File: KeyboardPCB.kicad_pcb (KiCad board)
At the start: 2 copper layers, 304.8 x 100 mm, 155 parts, among them J1 AVR-ISP-6, SW1 GRV, SW10 #9, SW11 #0, SW12 -_, SW13 =+, SW14 BSPC, SW15 PGUP, SW16 TAB, SW17 Q, SW18 W, SW19 E, SW2 #1, SW20 R, SW21 T, SW22 Y, SW23 U, SW24 I, SW25 O, SW26 P, SW27 [{, SW28 ]}, SW29 \|, SW3 #2, SW30 PGDN, SW31 CAPSLOCK, SW32 A, SW33 S, SW34 D, SW35 F, SW36 G, SW37 H, SW38 J, SW39 K, SW4 #3, SW40 L, SW41 ;:, SW42 '", SW43 ENTER, SW44 INS, SW45 LSHIFT, SW46 Z, SW47 X, SW48 C, SW49 V, SW5 #4, SW50 B, SW51 N, SW52 M, SW53 ,<, SW54 .>, SW55 /?, SW56 RSHIFT, SW57 UP, SW58 DEL, SW59 LCTRL, SW6 #5, SW60 LALT, SW61 LCOMMAND, SW62 SPACE, SW63 RCOMMAND, SW64 RALT, SW65 LEFT, SW66 DOWN, SW67 RIGHT, SW68 SW_SKQG, SW7 #6, SW8 #7, SW9 #8, U1 ATmega32U4-A, Y1 Crystal_GND24_Small

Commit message: Routed about half of the PCB
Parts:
- moved D27 11.0 mm to (287.3, 102.1)
- moved D30 11.0 mm to (353.2, 102.1)
- moved D20 11.0 mm to (153.2, 102.1)
- moved D21 11.0 mm to (172.2, 102.1)
- moved D22 11.0 mm to (191.3, 102.1)
- moved D23 11.0 mm to (210.3, 102.1)
- moved D24 11.0 mm to (229.4, 102.1)
- moved D25 11.0 mm to (248.4, 102.1)
- moved D16 11.0 mm to (72.2, 102.1)
- moved D17 11.0 mm to (96.0, 102.2)
- moved D18 11.0 mm to (115.1, 102.1)
- moved D19 11.0 mm to (134.1, 102.1)
- moved D26 11.0 mm to (268.3, 102.1)
- moved D28 11.0 mm to (305.6, 102.1)
- moved D29 11.0 mm to (329.4, 102.1)
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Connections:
- net Net-(D0-I/O1) renamed DP
- net Net-(D0-I/O2) renamed DN
- SW1 pad 1: Net-(D1-A) -> col0
- SW1 pad 2: col0 -> Net-(D1-A)
- SW10 pad 1: Net-(D10-A) -> col9
- SW10 pad 2: col9 -> Net-(D10-A)
- SW11 pad 1: Net-(D11-A) -> col10
- SW11 pad 2: col10 -> Net-(D11-A)
- SW12 pad 1: Net-(D12-A) -> col11
- SW12 pad 2: col11 -> Net-(D12-A)
- SW13 pad 1: Net-(D13-A) -> col12
- SW13 pad 2: col12 -> Net-(D13-A)
- SW14 pad 1: Net-(D14-A) -> col13
- SW14 pad 2: col13 -> Net-(D14-A)
- SW15 pad 1: Net-(D15-A) -> col14
- SW15 pad 2: col14 -> Net-(D15-A)
- SW16 pad 1: Net-(D16-A) -> col0
- SW16 pad 2: col0 -> Net-(D16-A)
- SW17 pad 1: Net-(D17-A) -> col1
- SW17 pad 2: col1 -> Net-(D17-A)
- SW18 pad 1: Net-(D18-A) -> col2
- SW18 pad 2: col2 -> Net-(D18-A)
- SW19 pad 1: Net-(D19-A) -> col3
- SW19 pad 2: col3 -> Net-(D19-A)
- SW2 pad 1: Net-(D2-A) -> col1
- SW2 pad 2: col1 -> Net-(D2-A)
- SW20 pad 1: Net-(D20-A) -> col4
- SW20 pad 2: col4 -> Net-(D20-A)
- SW21 pad 1: Net-(D21-A) -> col5
- SW21 pad 2: col5 -> Net-(D21-A)
- SW22 pad 1: Net-(D22-A) -> col6
- SW22 pad 2: col6 -> Net-(D22-A)
- SW23 pad 1: Net-(D23-A) -> col7
- SW23 pad 2: col7 -> Net-(D23-A)
- SW24 pad 1: Net-(D24-A) -> col8
- SW24 pad 2: col8 -> Net-(D24-A)
- SW25 pad 1: Net-(D25-A) -> col9
- SW25 pad 2: col9 -> Net-(D25-A)
- SW26 pad 1: Net-(D26-A) -> col10
- SW26 pad 2: col10 -> Net-(D26-A)
- SW27 pad 1: Net-(D27-A) -> col11
- SW27 pad 2: col11 -> Net-(D27-A)
- SW28 pad 1: Net-(D28-A) -> col12
- SW28 pad 2: col12 -> Net-(D28-A)
- SW29 pad 1: Net-(D29-A) -> col13
- SW29 pad 2: col13 -> Net-(D29-A)
- SW3 pad 1: Net-(D3-A) -> col2
- SW3 pad 2: col2 -> Net-(D3-A)
- SW30 pad 1: Net-(D30-A) -> col14
- SW30 pad 2: col14 -> Net-(D30-A)
- SW31 pad 1: Net-(D31-A) -> col0
- SW31 pad 2: col0 -> Net-(D31-A)
- SW32 pad 1: Net-(D32-A) -> col1
- SW32 pad 2: col1 -> Net-(D32-A)
- SW33 pad 1: Net-(D33-A) -> col2
- SW33 pad 2: col2 -> Net-(D33-A)
- SW34 pad 1: Net-(D34-A) -> col3
- SW34 pad 2: col3 -> Net-(D34-A)
- SW35 pad 1: Net-(D35-A) -> col4
- SW35 pad 2: col4 -> Net-(D35-A)
- SW36 pad 1: Net-(D36-A) -> col5
- SW36 pad 2: col5 -> Net-(D36-A)
- SW37 pad 1: Net-(D37-A) -> col6
- SW37 pad 2: col6 -> Net-(D37-A)
- SW38 pad 1: Net-(D38-A) -> col7
- SW38 pad 2: col7 -> Net-(D38-A)
- SW39 pad 1: Net-(D39-A) -> col8
- SW39 pad 2: col8 -> Net-(D39-A)
- SW4 pad 1: Net-(D4-A) -> col3
- SW4 pad 2: col3 -> Net-(D4-A)
- SW40 pad 1: Net-(D40-A) -> col9
- SW40 pad 2: col9 -> Net-(D40-A)
- SW41 pad 1: Net-(D41-A) -> col10
- SW41 pad 2: col10 -> Net-(D41-A)
- SW42 pad 1: Net-(D42-A) -> col11
- SW42 pad 2: col11 -> Net-(D42-A)
- SW43 pad 1: Net-(D43-A) -> col13
- SW43 pad 2: col13 -> Net-(D43-A)
- SW44 pad 1: Net-(D44-A) -> col14
- SW44 pad 2: col14 -> Net-(D44-A)
- SW45 pad 1: Net-(D45-A) -> col0
- SW45 pad 2: col0 -> Net-(D45-A)
- SW46 pad 1: Net-(D46-A) -> col1
- SW46 pad 2: col1 -> Net-(D46-A)
- SW47 pad 1: Net-(D47-A) -> col2
- SW47 pad 2: col2 -> Net-(D47-A)
- SW48 pad 1: Net-(D48-A) -> col3
- SW48 pad 2: col3 -> Net-(D48-A)
- SW49 pad 1: Net-(D49-A) -> col4
- SW49 pad 2: col4 -> Net-(D49-A)
- SW5 pad 1: Net-(D5-A) -> col4
- SW5 pad 2: col4 -> Net-(D5-A)
- SW50 pad 1: Net-(D50-A) -> col5
- SW50 pad 2: col5 -> Net-(D50-A)
- SW51 pad 1: Net-(D51-A) -> col6
- SW51 pad 2: col6 -> Net-(D51-A)
- SW52 pad 1: Net-(D52-A) -> col7
- SW52 pad 2: col7 -> Net-(D52-A)
- SW53 pad 1: Net-(D53-A) -> col8
- SW53 pad 2: col8 -> Net-(D53-A)
- SW54 pad 1: Net-(D54-A) -> col9
- SW54 pad 2: col9 -> Net-(D54-A)
- SW55 pad 1: Net-(D55-A) -> col10
- SW55 pad 2: col10 -> Net-(D55-A)
- SW56 pad 1: Net-(D56-A) -> col12
- SW56 pad 2: col12 -> Net-(D56-A)
- SW57 pad 1: Net-(D57-A) -> col13
- SW57 pad 2: col13 -> Net-(D57-A)
- SW58 pad 1: Net-(D58-A) -> col14
- SW58 pad 2: col14 -> Net-(D58-A)
- SW59 pad 1: Net-(D59-A) -> col0
- SW59 pad 2: col0 -> Net-(D59-A)
- SW6 pad 1: Net-(D6-A) -> col5
- SW6 pad 2: col5 -> Net-(D6-A)
- SW60 pad 1: Net-(D60-A) -> col1
- SW60 pad 2: col1 -> Net-(D60-A)
- SW61 pad 1: Net-(D61-A) -> col2
- SW61 pad 2: col2 -> Net-(D61-A)
- SW62 pad 1: Net-(D62-A) -> col6
- SW62 pad 2: col6 -> Net-(D62-A)
- SW63 pad 1: Net-(D63-A) -> col10
- SW63 pad 2: col10 -> Net-(D63-A)
- SW64 pad 1: Net-(D64-A) -> col11
- SW64 pad 2: col11 -> Net-(D64-A)
- SW65 pad 1: Net-(D65-A) -> col12
- SW65 pad 2: col12 -> Net-(D65-A)
- SW66 pad 1: Net-(D66-A) -> col13
- SW66 pad 2: col13 -> Net-(D66-A)
- SW67 pad 1: Net-(D67-A) -> col14
- SW67 pad 2: col14 -> Net-(D67-A)
- SW7 pad 1: Net-(D7-A) -> col6
- SW7 pad 2: col6 -> Net-(D7-A)
- SW8 pad 1: Net-(D8-A) -> col7
- SW8 pad 2: col7 -> Net-(D8-A)
- SW9 pad 1: Net-(D9-A) -> col8
- SW9 pad 2: col8 -> Net-(D9-A)
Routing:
- net row0: track 0.00 -> 268.9 mm
- net row1: track 0.00 -> 261.9 mm
- net row2: track 0.00 -> 259.6 mm
- net row3: track 0.00 -> 254.9 mm
- net row4: track 0.00 -> 209.7 mm
- net col1: track 0.00 -> 90.9 mm
- net col10: track 0.00 -> 89.9 mm
- net col2: track 0.00 -> 88.0 mm
- net col6: track 0.00 -> 87.9 mm
- net col13: track 0.00 -> 86.1 mm
- net col11: track 0.00 -> 84.4 mm
- net col0: track 0.00 -> 84.1 mm
- net col12: track 0.00 -> 84.0 mm
- net col14: track 0.00 -> 76.2 mm
- net DP: track 0.00 -> 73.9 mm
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- added copper zone on B.Cu, net GND
- added copper zone on F.Cu, net GND

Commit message: Routed around MCU
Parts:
- removed C6: 0.1u, Capacitor_SMD:C_0805_2012Metric
- moved D9 11.5 mm to (219.6, 83.6)
- moved R1 3.25 mm to (210.6, 162.8)
- moved C2 2.27 mm to (231.3, 156.5)
- moved Y1 2.27 mm to (227.8, 155.4)
- moved C3 2.27 mm to (231.3, 154.3)
- moved C7 1.75 mm to (227.8, 151.0), turned to 0 degrees
- moved C8 1.02 mm to (208.3, 145.8)
- moved C5 0.56 mm to (206.6, 158.2), turned to 90 degrees
- turned R5 to 0 degrees
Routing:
- net GND: track 23.5 -> 180.1 mm, vias 3 -> 8
- net +5V: track 5.85 -> 149.6 mm, vias 0 -> 6
- net VCC: track 0.00 -> 22.4 mm, vias 0 -> 2
- net row2: track 259.6 -> 278.6 mm, vias 0 -> 2
- net row0: track 268.9 -> 287.5 mm, vias 0 -> 2
- net Net-(USB1-CC1): track 0.00 -> 6.13 mm
- net Net-(USB1-CC2): track 0.00 -> 5.88 mm
- net Net-(D9-A): track 11.5 -> 6.52 mm
- net Net-(U1-UCAP): track 0.00 -> 4.38 mm
- net col8: track 66.9 -> 69.2 mm
- net XTAL1: track 12.4 -> 10.6 mm
- net XTAL2: track 11.0 -> 9.15 mm

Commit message: Continued routing
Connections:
- U1 pad 1: row0 -> row3
- U1 pad 36: col6 -> row4
- U1 pad 38: row1 -> col6
- U1 pad 39: row4 -> row0
- U1 pad 40: row3 -> row1
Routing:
- net col0: track 84.1 -> 247.0 mm, vias 0 -> 1
- net col14: track 76.2 -> 215.5 mm, vias 0 -> 1
- net col1: track 90.9 -> 225.6 mm, vias 0 -> 1
- net col13: track 86.1 -> 204.9 mm, vias 0 -> 1
- net col2: track 88.0 -> 194.7 mm, vias 0 -> 1
- net col12: track 84.0 -> 179.5 mm, vias 0 -> 1
- net col3: track 66.9 -> 156.7 mm, vias 0 -> 1
- net row4: track 209.7 -> 295.2 mm, vias 0 -> 2
- net col11: track 84.4 -> 161.8 mm, vias 0 -> 1
- net col4: track 66.9 -> 136.5 mm, vias 0 -> 1
- net col9: track 66.9 -> 115.4 mm, vias 0 -> 1
- net col10: track 89.9 -> 136.7 mm, vias 0 -> 1
- net col5: track 66.9 -> 113.4 mm, vias 0 -> 1
- net col8: track 69.2 -> 108.4 mm, vias 0 -> 1
- net row3: track 254.9 -> 289.8 mm, vias 0 -> 4
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
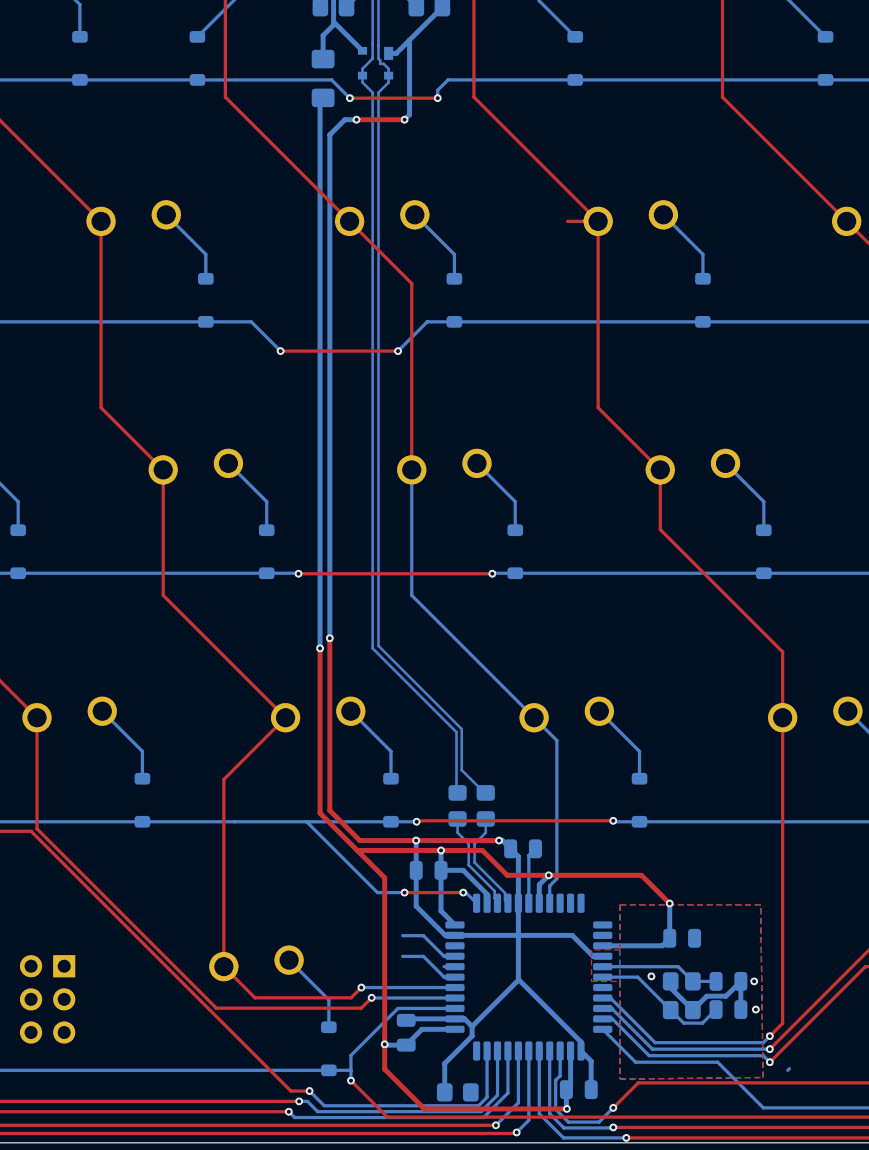
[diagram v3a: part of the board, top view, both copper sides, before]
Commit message: Finished Keyboard Matrix routing
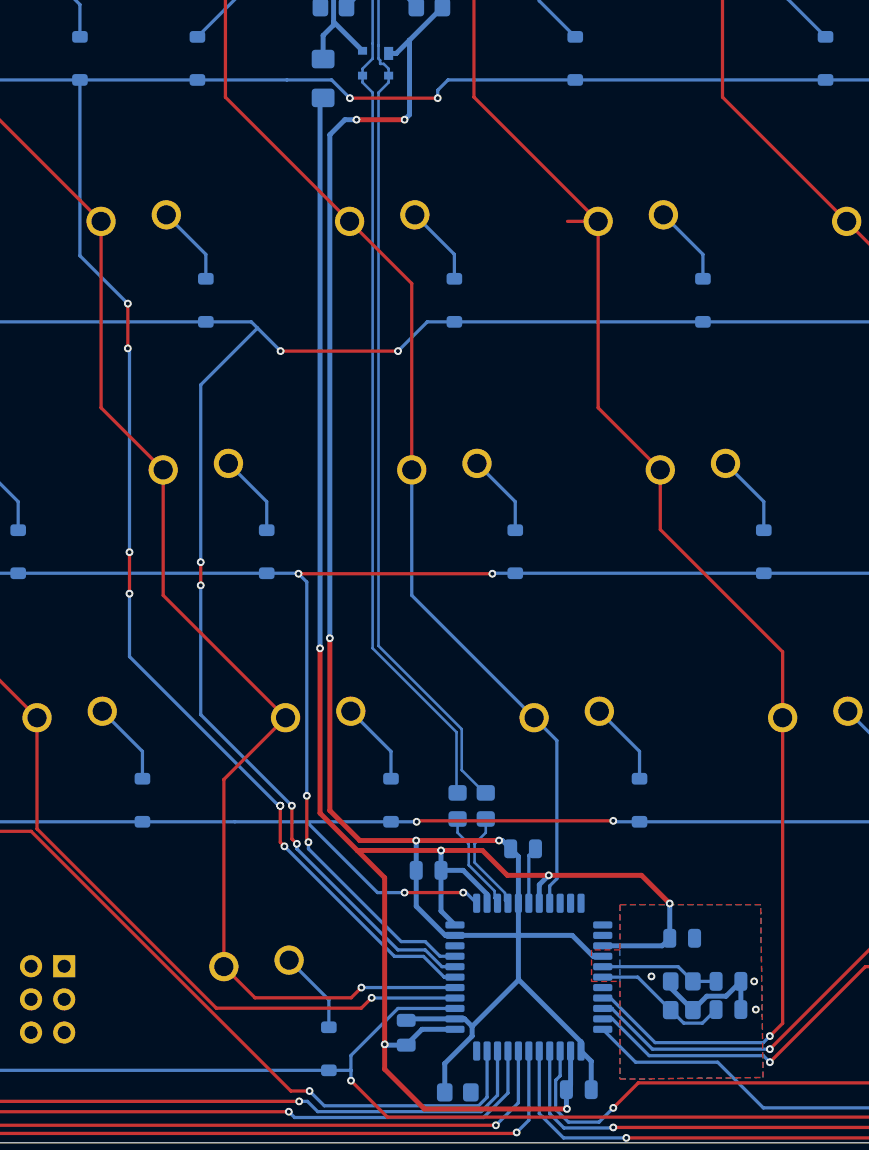
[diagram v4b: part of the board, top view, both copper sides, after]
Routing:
- net row0: track 292.1 -> 370.1 mm, vias 2 -> 9
- net row1: track 283.7 -> 343.5 mm, vias 2 -> 6
- net row2: track 283.3 -> 314.7 mm, vias 2 -> 4
